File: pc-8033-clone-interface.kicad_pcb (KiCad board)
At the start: 2 copper layers, 95.2 x 67.3 mm, 20 parts, among them J2 80s31, U2 74LS32, U3 74LS04, U4 82C55A, U5 74LS30

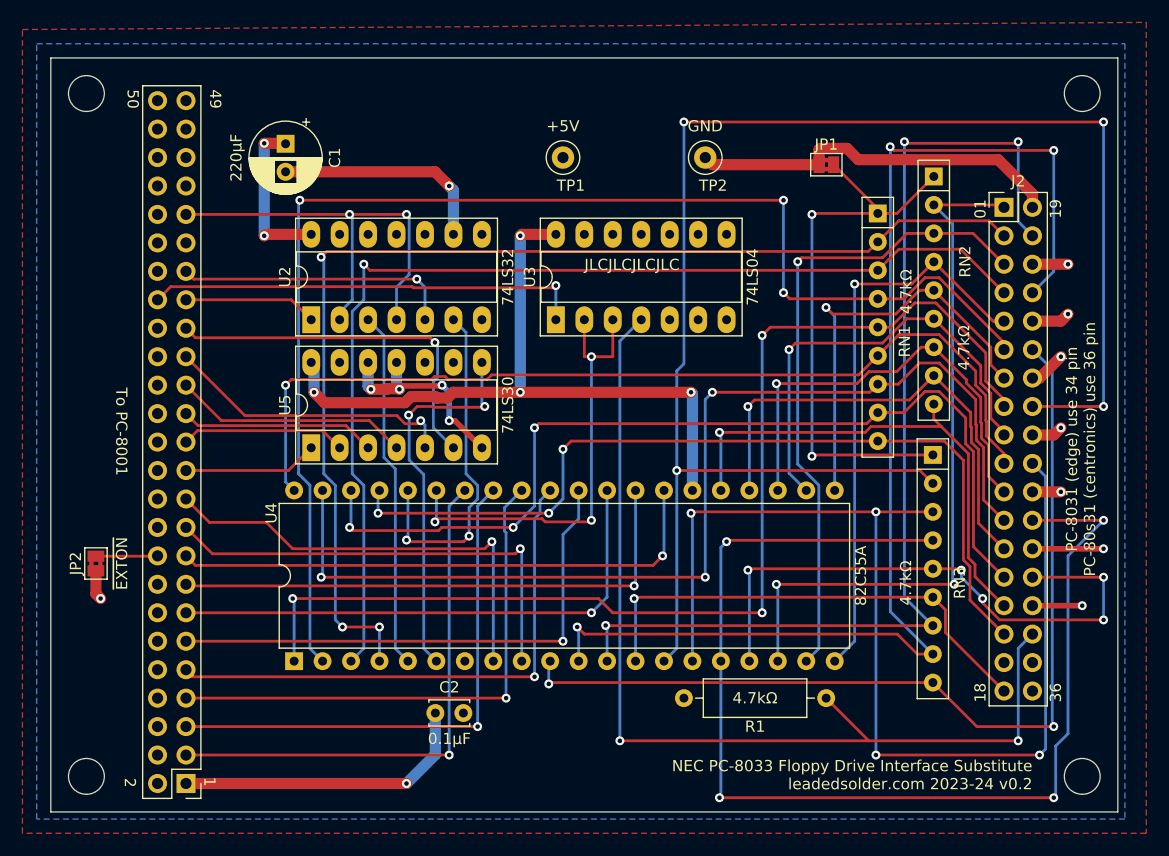
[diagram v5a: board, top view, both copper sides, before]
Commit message: V3: fix the pinout once and for all
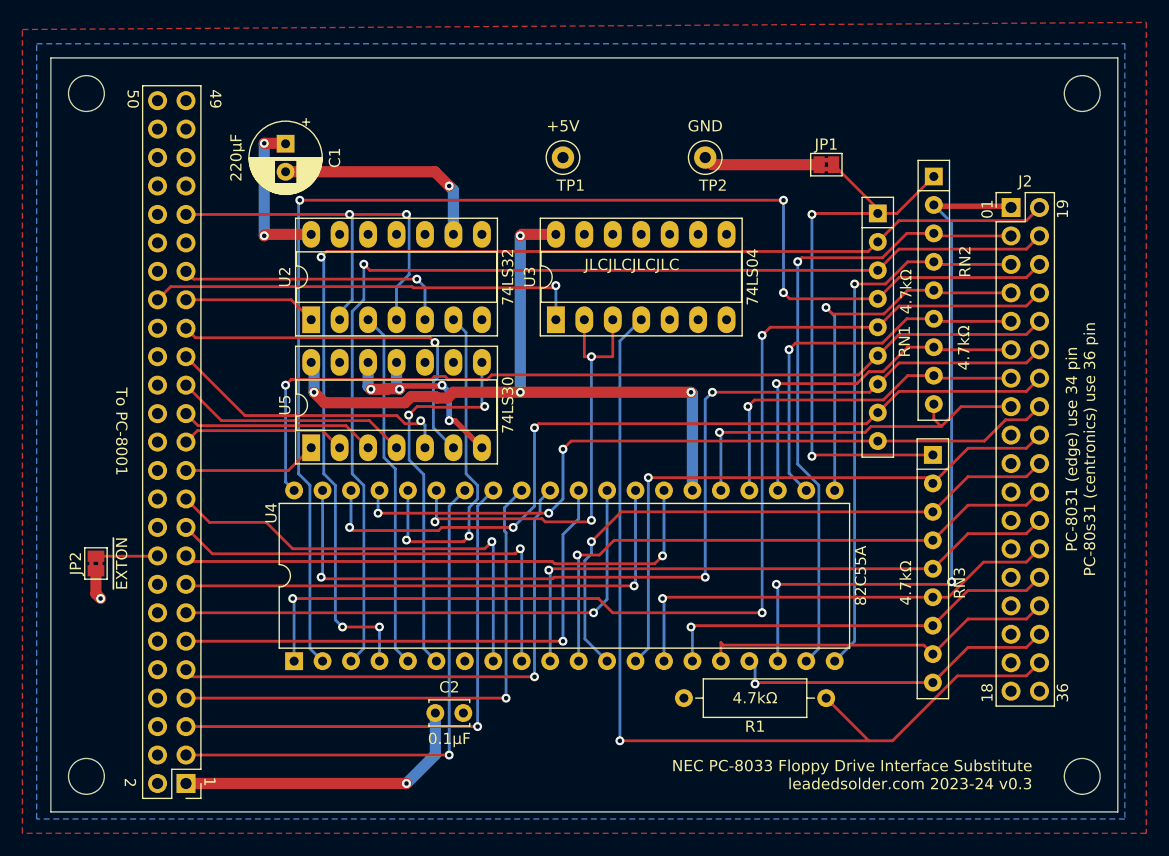
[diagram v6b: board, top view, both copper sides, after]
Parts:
- moved J2 0.63 mm to (190.5, 84.5)
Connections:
- J2 pad 10: /pa4 -> GND
- J2 pad 11: /pb5 -> GND
- J2 pad 12: /pa5 -> GND
- J2 pad 13: /pb6 -> GND
- J2 pad 14: /pa6 -> GND
- J2 pad 15: /pb7 -> GND
- J2 pad 16: /pa7 -> GND
- J2 pad 18: /pc4 -> GND
- J2 pad 19: GND -> /pa0
- J2 pad 2: /pa0 -> /pb1
- J2 pad 20: /pc5 -> /pa1
- J2 pad 21: GND -> /pa2
- J2 pad 22: /pc6 -> /pa3
- J2 pad 23: GND -> /pa4
- J2 pad 24: /pc7 -> /pa5
- J2 pad 25: GND -> /pa6
- J2 pad 26: /pc0 -> /pa7
- J2 pad 27: GND -> /pc4
- J2 pad 28: /pc1 -> /pc5
- J2 pad 29: GND -> /pc6
- J2 pad 3: /pb1 -> /pb2
- J2 pad 30: /pc2 -> /pc7
- J2 pad 31: GND -> /pc0
- J2 pad 32: /pc3 -> /pc1
- J2 pad 33: GND -> /pc2
- J2 pad 34: Net-(J2-Pin_34) -> /pc3
- J2 pad 35: GND -> Net-(J2-Pin_35)
- J2 pad 4: /pa1 -> /pb3
- J2 pad 5: /pb2 -> /pb4
- J2 pad 6: /pa2 -> /pb5
- J2 pad 7: /pb3 -> /pb6
- J2 pad 8: /pa3 -> /pb7
- J2 pad 9: /pb4 -> GND
- R1 pad 2: Net-(J2-Pin_34) -> Net-(J2-Pin_35)
- RN3 pad 2: /pc0 -> /pc4
- RN3 pad 3: /pc1 -> /pc5
- RN3 pad 4: /pc2 -> /pc6
- RN3 pad 5: /pc3 -> /pc7
- RN3 pad 6: /pc4 -> /pc0
- RN3 pad 7: /pc5 -> /pc1
- RN3 pad 8: /pc6 -> /pc2
- RN3 pad 9: /pc7 -> /pc3
- U3 pad 4: Net-(J2-Pin_34) -> Net-(J2-Pin_35)
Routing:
- net /pc0: track 141.4 -> 41.1 mm, vias 4 -> 1
- net Net-(J2-Pin_34): track 89.4 -> 0.00 mm, vias 2 -> 0
- net Net-(J2-Pin_35): track 0.00 -> 84.1 mm, vias 0 -> 1
- net /pc2: track 104.4 -> 32.3 mm, vias 4 -> 0
- net /pc1: track 98.0 -> 36.0 mm, vias 4 -> 1
- net /pc6: track 110.9 -> 53.1 mm, vias 3 -> 1
- net GND: track 101.0 -> 51.6 mm, vias 13 -> 6
- net /pc5: track 95.9 -> 54.6 mm, vias 3 -> 1
- net /pc7: track 83.3 -> 53.8 mm, vias 2 -> 1
- net /pc3: track 52.6 -> 29.5 mm, vias 5 -> 1
- net /pb7: track 45.8 -> 34.5 mm
- net /pb6: track 43.3 -> 32.3 mm
- net /pc4: track 43.4 -> 53.8 mm
- net /pa7: track 77.3 -> 67.7 mm
- net /pa6: track 84.3 -> 74.8 mm
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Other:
- board text added: "NEC PC-8033 Floppy Drive Interface Substitute leadedsolder.com 2023-24 v0.3"
- board text removed: "NEC PC-8033 Floppy Drive Interface Substitute leadedsolder.com 2023-24 v0.2"

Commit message: Fix select logic
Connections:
- U5 pad 11: GND -> +5V
- U5 pad 12: GND -> +5V
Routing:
- net +5V: track 104.8 -> 114.3 mm
- net GND: track 51.6 -> 47.6 mm
- net /pa4: track 79.6 -> 80.5 mm
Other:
- board text added: "NEC PC-8033 Floppy Drive Interface Substitute leadedsolder.com 2023-24 v0.4"
- board text removed: "NEC PC-8033 Floppy Drive Interface Substitute leadedsolder.com 2023-24 v0.3"

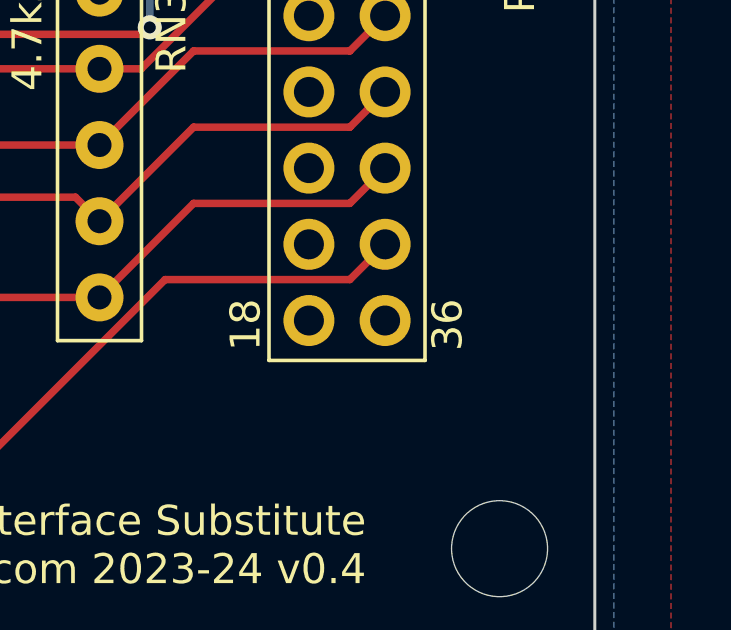
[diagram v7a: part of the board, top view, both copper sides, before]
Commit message: Add header pin numbers to the underside for kicks
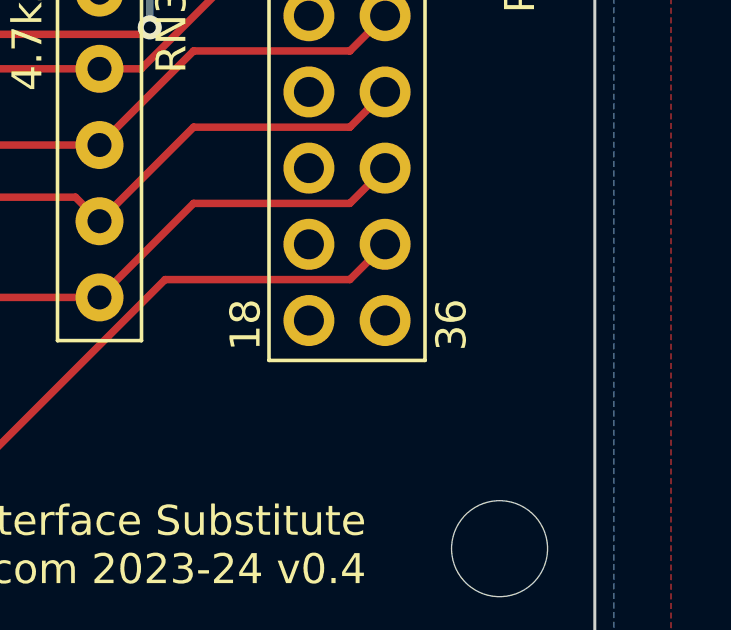
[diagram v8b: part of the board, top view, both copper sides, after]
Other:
- board text added: "01"
- board text added: "18"
- board text added: "19"
- board text added: "36"
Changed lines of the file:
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@@
         (effects (font (size 1 1) (thickness 0.1)) (justify left bottom))
     )
-    (fp_text user "36" (at 5.207 44.196 90 unlocked) (layer "F.SilkS")
+    (fp_text user "36" (at 5.339 44.196 90 unlocked) (layer "F.SilkS")
         (effects (font (size 1 1) (thickness 0.1)) (justify left bottom))
     )
@@
   (gr_rect (start 104.775 71.12) (end 200.025 138.43)
     (stroke (width 0.1) (type default)) (fill none) (layer "Edge.Cuts"))
+  (gr_text "18" (at 187.706 128.524 -90) (layer "B.SilkS")
+    (effects (font (size 1 1) (thickness 0.1)) (justify left bottom mirror))
+  )
+  (gr_text "01" (at 187.706 85.344 -90) (layer "B.SilkS")
+    (effects (font (size 1 1) (thickness 0.1)) (justify left bottom mirror))
+  )
+  (gr_text "19" (at 194.564 85.344 -90) (layer "B.SilkS")
+    (effects (font (size 1 1) (thickness 0.1)) (justify left bottom mirror))
+  )
+  (gr_text "36" (at 194.365 128.524 -90) (layer "B.SilkS")
+    (effects (font (size 1 1) (thickness 0.1)) (justify left bottom mirror))
+  )
+  (gr_text "1" (at 119.634 135.28881 90) (layer "B.SilkS")
+    (effects (font (size 1 1) (thickness 0.15)) (justify left bottom mirror))
+  )
+  (gr_text "49" (at 120.015 73.914 90) (layer "B.SilkS")
+    (effects (font (size 1 1) (thickness 0.15)) (justify left bottom mirror))
+  )
+  (gr_text "50" (at 112.395 73.914 90) (layer "B.SilkS")
+    (effects (font (size 1 1) (thickness 0.15)) (justify left bottom mirror))
+  )
+  (gr_text "2" (at 112.522 135.382 90) (layer "B.SilkS")
+    (effects (font (size 1 1) (thickness 0.15)) (justify left bottom mirror))
+  )
   (gr_text "1" (at 118.364 135.28881 -90) (layer "F.SilkS")
     (effects (font (size 1 1) (thickness 0.15)) (justify left bottom))
